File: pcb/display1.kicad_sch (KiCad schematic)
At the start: 20 parts, among them Q1 DMG2301L, Q2 DMG2301L, Q3 DMG2301L, Q4 DMG2301L, U2 TPIC6C596

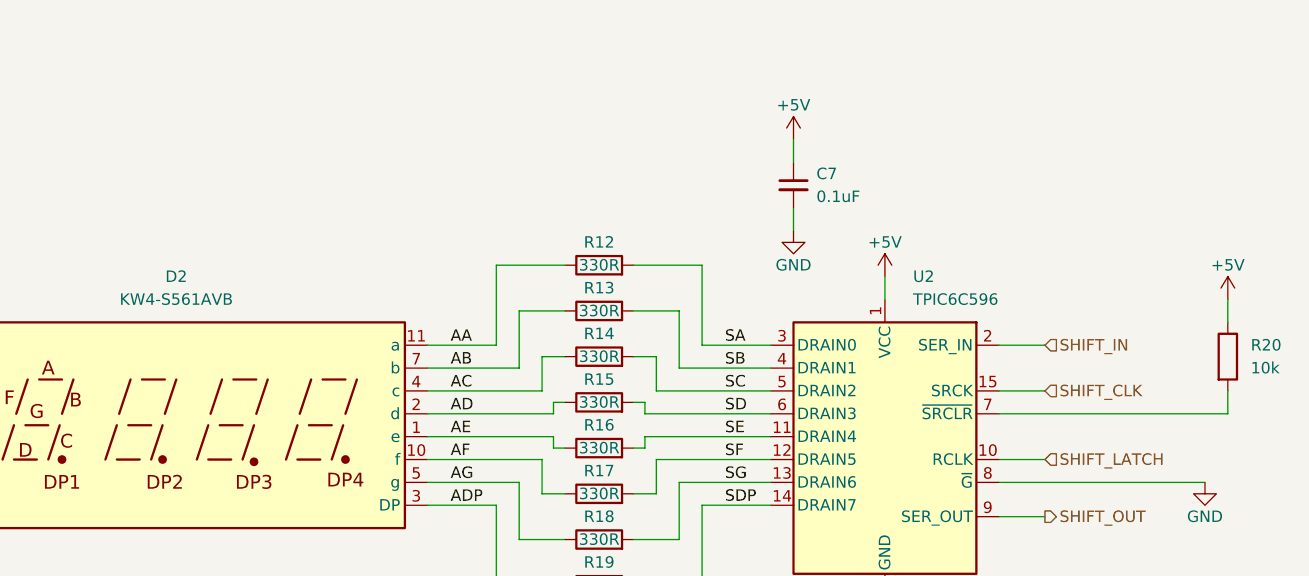
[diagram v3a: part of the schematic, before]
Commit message: start to route display traces
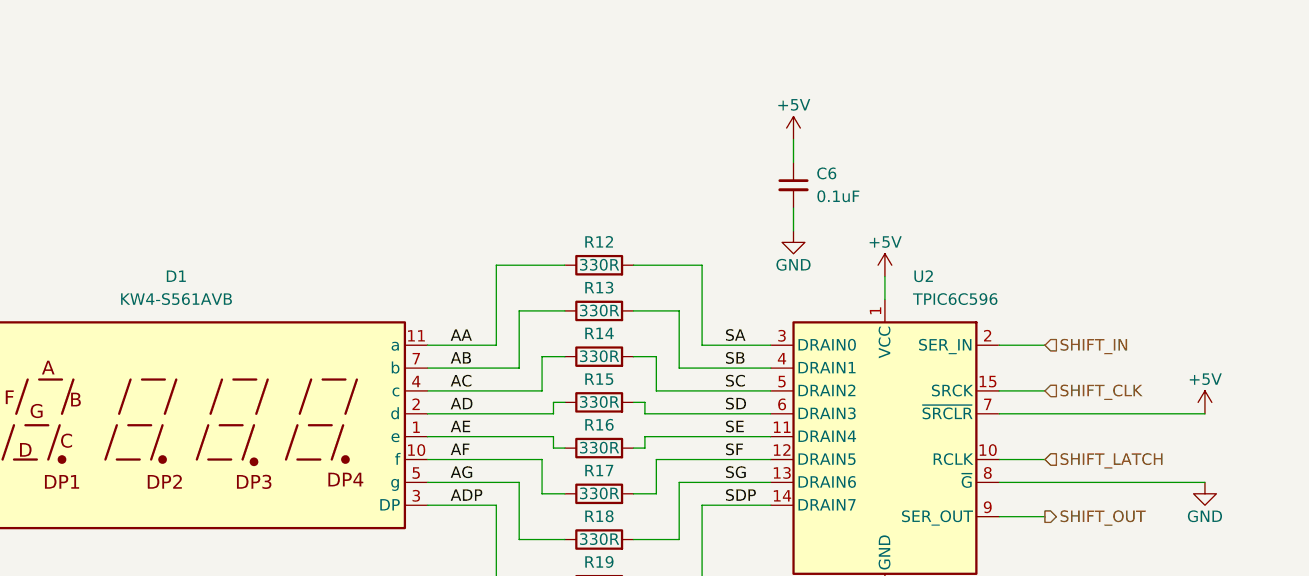
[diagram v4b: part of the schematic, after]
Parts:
- removed R20: 10k, Resistor_SMD:R_0805_2012Metric_Pad1.20x1.40mm_HandSolder, symbol Device:R
- renumbered C7 to C6, D2 to D1
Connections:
- net +5V: now also U2.7 (~{SRCLR})
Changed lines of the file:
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@@
-	(wire
-		(pts
-			(xy 248.92 68.58) (xy 248.92 71.12)
-		)
-		(stroke
-			(width 0)
-			(type default)
-		)
-	)
 	(wire
 		(pts
@@
 	(wire
 		(pts
-			(xy 248.92 78.74) (xy 248.92 81.28)
-		)
-		(stroke
-			(width 0)
-			(type default)
-		)
-	)
-	(wire
-		(pts
 			(xy 160.02 76.2) (xy 170.18 76.2)
 		)
@@
 	(wire
 		(pts
-			(xy 248.92 81.28) (xy 223.52 81.28)
+			(xy 246.38 81.28) (xy 223.52 81.28)
 		)
 		(stroke
@@
 		(on_board yes)
 		(dnp no)
-		(property "Reference" "#PWR036"
+		(property "Reference" "#PWR038"
 			(at 210.82 110.49 0)
 			(effects
@@
 			(project ""
 				(path "/1883df74-0bd5-446c-9076-f848bb3cfebf/783ca70e-2b43-402c-8078-60ba3aaea8cd"
-					(reference "#PWR036")
+					(reference "#PWR038")
 					(unit 1)
 				)
@@
 		(on_board yes)
 		(dnp no)
-		(property "Reference" "#PWR037"
+		(property "Reference" "#PWR040"
 			(at 246.38 95.25 0)
 			(effects
@@
 			(project "mtg_life_counter"
 				(path "/1883df74-0bd5-446c-9076-f848bb3cfebf/783ca70e-2b43-402c-8078-60ba3aaea8cd"
-					(reference "#PWR037")
+					(reference "#PWR040")
 					(unit 1)
 				)
@@
 		(dnp no)
 		(fields_autoplaced yes)
-		(property "Reference" "D2"
+		(property "Reference" "D1"
 			(at 132.08 66.04 0)
 			(effects
@@
 			(project ""
 				(path "/1883df74-0bd5-446c-9076-f848bb3cfebf/783ca70e-2b43-402c-8078-60ba3aaea8cd"
-					(reference "D2")
+					(reference "D1")
 					(unit 1)
 				)
@@
 		(on_board yes)
 		(dnp no)
-		(property "Reference" "#PWR035"
+		(property "Reference" "#PWR037"
 			(at 210.82 69.85 0)
 			(effects
@@
 			(project ""
 				(path "/1883df74-0bd5-446c-9076-f848bb3cfebf/783ca70e-2b43-402c-8078-60ba3aaea8cd"
-					(reference "#PWR035")
+					(reference "#PWR037")
 					(unit 1)
 				)
@@
 	)
 	(symbol
-		(lib_id "Device:R")
-		(at 248.92 74.93 0)
-		(unit 1)
-		(exclude_from_sim no)
-		(in_bom yes)
-		(on_board yes)
-		(dnp no)
-		(fields_autoplaced yes)
-		(property "Reference" "R20"
-			(at 251.46 73.6599 0)
-			(effects
-				(font
-					(size 1.27 1.27)
-				)
-				(justify left)
-			)
-		)
-		(property "Value" "10k"
-			(at 251.46 76.1999 0)
-			(effects
-				(font
-					(size 1.27 1.27)
-				)
-				(justify left)
-			)
-		)
-		(property "Footprint" "Resistor_SMD:R_0805_2012Metric_Pad1.20x1.40mm_HandSolder"
-			(at 247.142 74.93 90)
-			(effects
-				(font
-					(size 1.27 1.27)
-				)
-				(hide yes)
-			)
-		)
-		(property "Datasheet" "~"
-			(at 248.92 74.93 0)
-			(effects
-				(font
-					(size 1.27 1.27)
-				)
-				(hide yes)
-			)
-		)
-		(property "Description" "Resistor"
-			(at 248.92 74.93 0)
-			(effects
-				(font
-					(size 1.27 1.27)
-				)
-				(hide yes)
-			)
-		)
-		(pin "1"
-		)
-		(pin "2"
-		)
-		(instances
-			(project ""
-				(path "/1883df74-0bd5-446c-9076-f848bb3cfebf/783ca70e-2b43-402c-8078-60ba3aaea8cd"
-					(reference "R20")
-					(unit 1)
-				)
-			)
-		)
-	)
-	(symbol
 		(lib_id "Transistor_FET:DMG2301L")
 		(at 60.96 33.02 0)
@@
 		(on_board yes)
 		(dnp no)
-		(property "Reference" "#PWR066"
+		(property "Reference" "#PWR036"
 			(at 200.66 67.31 0)
 			(effects
@@
 			(project "mtg_life_counter"
 				(path "/1883df74-0bd5-446c-9076-f848bb3cfebf/783ca70e-2b43-402c-8078-60ba3aaea8cd"
-					(reference "#PWR066")
+					(reference "#PWR036")
 					(unit 1)
 				)
@@
 	(symbol
 		(lib_id "power:+5V")
-		(at 248.92 68.58 0)
-		(unit 1)
-		(exclude_from_sim no)
-		(in_bom yes)
-		(on_board yes)
-		(dnp no)
-		(property "Reference" "#PWR038"
-			(at 248.92 72.39 0)
+		(at 246.38 81.28 0)
+		(unit 1)
+		(exclude_from_sim no)
+		(in_bom yes)
+		(on_board yes)
+		(dnp no)
+		(property "Reference" "#PWR039"
+			(at 246.38 85.09 0)
 			(effects
 				(font
@@
 		)
 		(property "Value" "+5V"
-			(at 248.92 64.77 0)
+			(at 246.38 77.47 0)
 			(effects
 				(font
@@
 		)
 		(property "Footprint" ""
-			(at 248.92 68.58 0)
+			(at 246.38 81.28 0)
 			(effects
 				(font
@@
 		)
 		(property "Datasheet" ""
-			(at 248.92 68.58 0)
+			(at 246.38 81.28 0)
 			(effects
 				(font
@@
 		)
 		(property "Description" "Power symbol creates a global label with name \"+5V\""
-			(at 248.92 68.58 0)
+			(at 246.38 81.28 0)
 			(effects
 				(font
@@
 			(project "mtg_life_counter"
 				(path "/1883df74-0bd5-446c-9076-f848bb3cfebf/783ca70e-2b43-402c-8078-60ba3aaea8cd"
-					(reference "#PWR038")
+					(reference "#PWR039")
 					(unit 1)
 				)
@@
 		(dnp no)
 		(fields_autoplaced yes)
-		(property "Reference" "C7"
+		(property "Reference" "C6"
 			(at 203.2 54.6162 0)
 			(effects
@@
 			(project "mtg_life_counter"
 				(path "/1883df74-0bd5-446c-9076-f848bb3cfebf/783ca70e-2b43-402c-8078-60ba3aaea8cd"
-					(reference "C7")
+					(reference "C6")
 					(unit 1)
 				)
@@
 		(on_board yes)
 		(dnp no)
-		(property "Reference" "#PWR065"
+		(property "Reference" "#PWR035"
 			(at 200.66 54.61 0)
 			(effects
@@
 			(project "mtg_life_counter"
 				(path "/1883df74-0bd5-446c-9076-f848bb3cfebf/783ca70e-2b43-402c-8078-60ba3aaea8cd"
-					(reference "#PWR065")
-					(unit 1)
-				)
+					(reference "#PWR035")
+					(unit 1)
+				)

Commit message: continue layout. improve 3d model
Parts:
- D1: footprint mtg_life_counter:KW4-S561xxB_SMD -> mtg_life_counter:KW4-S561xVB_SMD
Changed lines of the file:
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@@
 			)
 		)
-		(property "Footprint" "mtg_life_counter:KW4-S561xxB_SMD"
+		(property "Footprint" "mtg_life_counter:KW4-S561xVB_SMD"
 			(at 132.08 95.25 0)
 			(effects

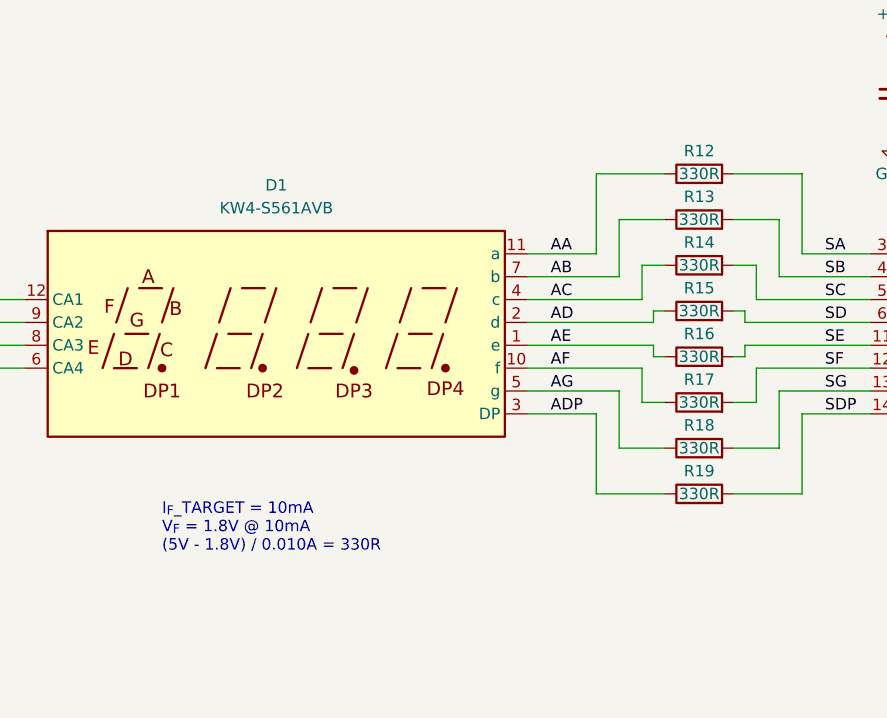
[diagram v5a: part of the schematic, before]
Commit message: continue layout. update leds for KD4 led modules
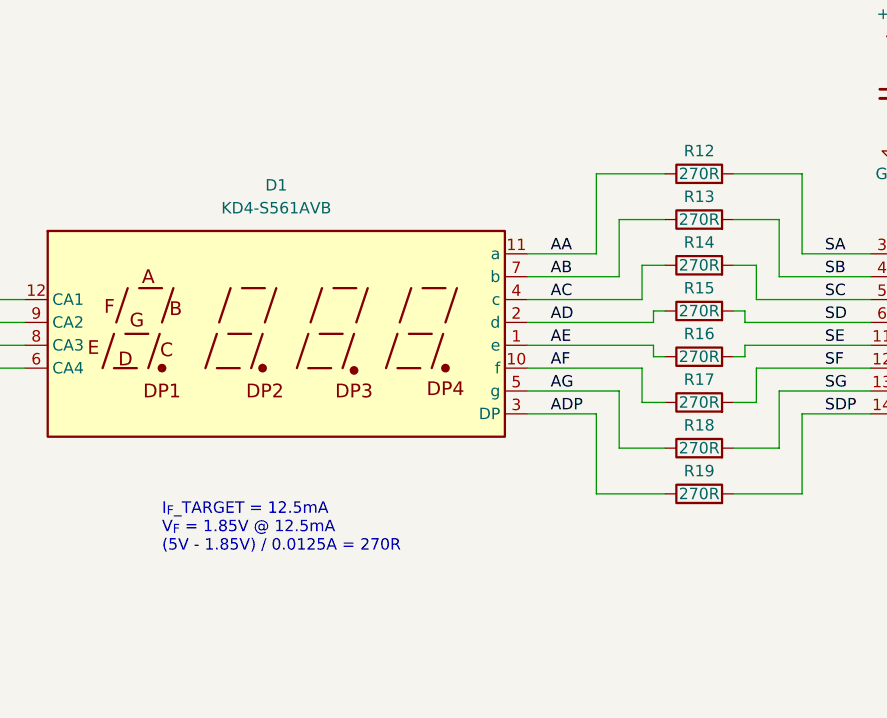
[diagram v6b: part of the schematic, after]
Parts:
- D1: value KW4-S561AVB -> KD4-S561AVB; footprint mtg_life_counter:KW4-S561xVB_SMD -> mtg_life_counter:KD4-S561xxB_SMD_Slim
- R12, R13, R14, R15, R16, R17, R18, R19: value 330R -> 270R
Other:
- note added: "I_{F}_TARGET = 12.5mA V_{F} = 1.85V @ 12.5mA (5V - 1.85V) / 0.0125A = 270R"
- note removed: "I_{F}_TARGET = 10mA V_{F} = 1.8V @ 10mA (5V - 1.8V) / 0.010A = 330R"
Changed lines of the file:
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@@
 		(company "Max Proskauer")
 	)
-	(text "I_{F}_TARGET = 10mA\nV_{F} = 1.8V @ 10mA\n(5V - 1.8V) / 0.010A = 330R"
+	(text "I_{F}_TARGET = 12.5mA\nV_{F} = 1.85V @ 12.5mA\n(5V - 1.85V) / 0.0125A = 270R"
 		(exclude_from_sim no)
 		(at 119.38 104.14 0)
@@
 			)
 		)
-		(property "Value" "330R"
+		(property "Value" "270R"
 			(at 179.07 80.01 90)
 			(effects
@@
 			)
 		)
-		(property "Value" "330R"
+		(property "Value" "270R"
 			(at 179.07 95.25 90)
 			(effects
@@
 			)
 		)
-		(property "Value" "KW4-S561AVB"
+		(property "Value" "KD4-S561AVB"
 			(at 132.08 68.58 0)
 			(effects
@@
 			)
 		)
-		(property "Footprint" "mtg_life_counter:KW4-S561xVB_SMD"
+		(property "Footprint" "mtg_life_counter:KD4-S561xxB_SMD_Slim"
 			(at 132.08 95.25 0)
 			(effects
@@
 			)
 		)
-		(property "Value" "330R"
+		(property "Value" "270R"
 			(at 179.07 74.93 90)
 			(effects
@@
 			)
 		)
-		(property "Value" "330R"
+		(property "Value" "270R"
 			(at 179.07 85.09 90)
 			(effects
@@
 			)
 		)
-		(property "Value" "330R"
+		(property "Value" "270R"
 			(at 179.07 90.17 90)
 			(effects
@@
 			)
 		)
-		(property "Value" "330R"
+		(property "Value" "270R"
 			(at 179.07 64.77 90)
 			(effects
@@
 			)
 		)
-		(property "Value" "330R"
+		(property "Value" "270R"
 			(at 179.07 69.85 90)
 			(effects
@@
 			)
 		)
-		(property "Value" "330R"
+		(property "Value" "270R"
 			(at 179.07 100.33 90)
 			(effects
